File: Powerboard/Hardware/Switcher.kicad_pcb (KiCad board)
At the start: 4 copper layers, 47 x 50 mm, 118 parts, among them IC2 SiC437BED-T1-GE3, J1 Conn_01x03_MountingPin, J2 XT60PW-F, J3 USB_C_Receptacle_USB2.0, J4 Conn_01x02_Male, J5 Conn_01x08_Male, J6 Conn_01x02_Male, J7 XT60PW-M, J8 Conn_01x04_Male, Q1 PXP012-30QLJ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

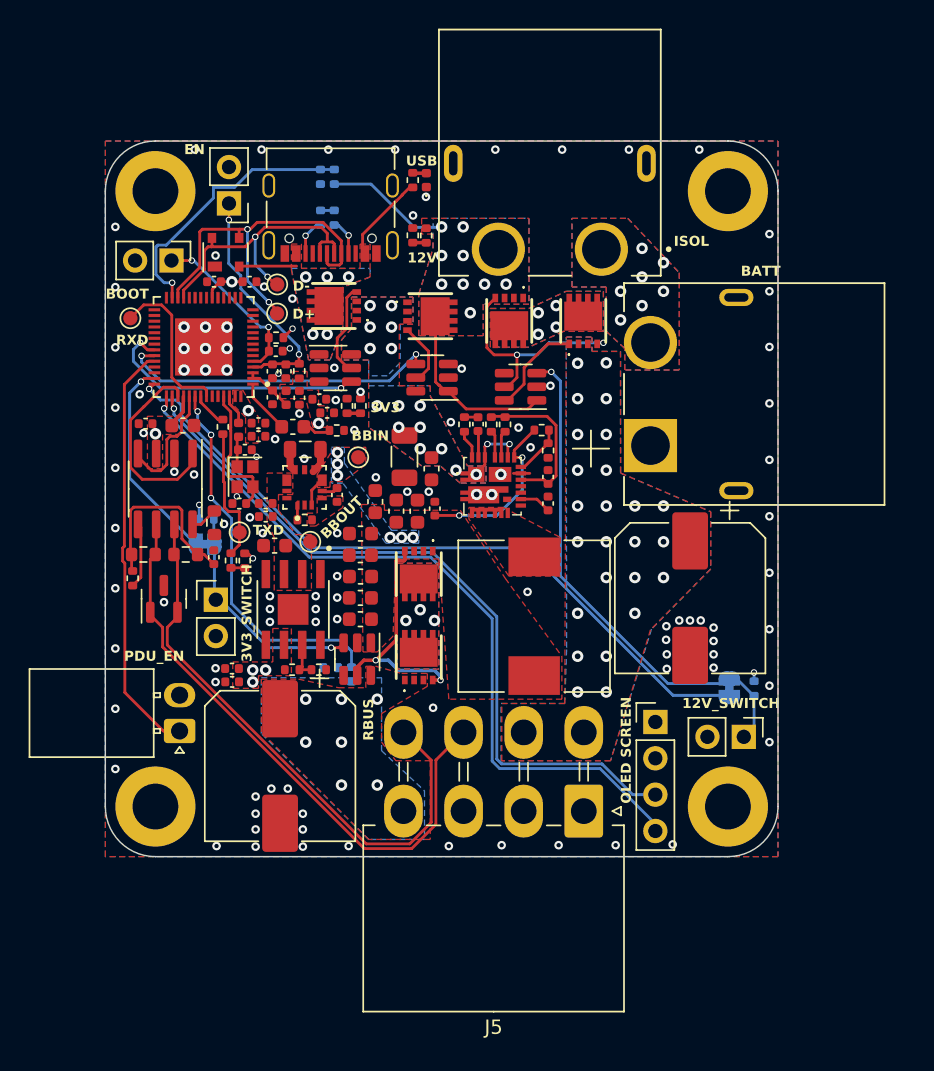
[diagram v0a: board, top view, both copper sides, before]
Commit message: mosfet flipping
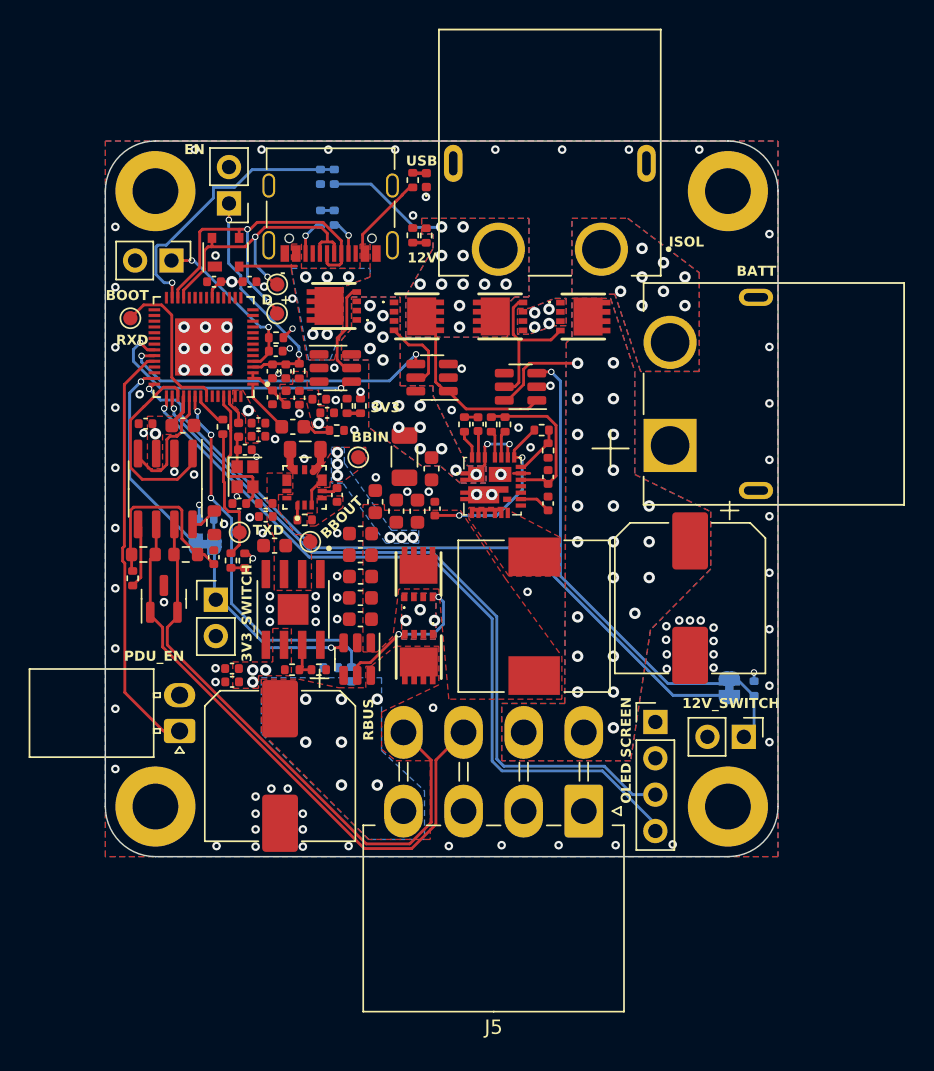
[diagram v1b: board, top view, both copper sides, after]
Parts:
- moved J7 1.37 mm to (112.0, 40.7)
- moved Q5 0.94 mm to (88.3, 35.2)
- moved Q4 0.71 mm to (94.1, 35.3), turned to 90 degrees
- moved Q3 0.31 mm to (99.9, 35.3), turned to -90 degrees
- turned Q2 to 0 degrees
- turned Q1 to 180 degrees
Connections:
- Q1 pad 1: Net-(J5-Pin_4) -> Net-(Q1-S_1)
- Q1 pad 2: Net-(J5-Pin_4) -> Net-(Q1-S_1)
- Q1 pad 3: Net-(J5-Pin_4) -> Net-(Q1-S_1)
- Q1 pad 5: Net-(Q1-D_1) -> Net-(J5-Pin_4)
- Q1 pad 6: Net-(Q1-D_1) -> Net-(J5-Pin_4)
- Q1 pad 7: Net-(Q1-D_1) -> Net-(J5-Pin_4)
- Q1 pad 8: Net-(Q1-D_1) -> Net-(J5-Pin_4)
- Q1 pad 9: Net-(Q1-D_1) -> Net-(J5-Pin_4)
- Q2 pad 1: RBUS_uC_V -> Net-(Q1-S_1)
- Q2 pad 2: RBUS_uC_V -> Net-(Q1-S_1)
- Q2 pad 3: RBUS_uC_V -> Net-(Q1-S_1)
- Q2 pad 5: Net-(Q1-D_1) -> RBUS_uC_V
- Q2 pad 6: Net-(Q1-D_1) -> RBUS_uC_V
- Q2 pad 7: Net-(Q1-D_1) -> RBUS_uC_V
- Q2 pad 8: Net-(Q1-D_1) -> RBUS_uC_V
- Q2 pad 9: Net-(Q1-D_1) -> RBUS_uC_V
- Q3 pad 1: Net-(J5-Pin_5) -> Net-(Q3-S_1)
- Q3 pad 2: Net-(J5-Pin_5) -> Net-(Q3-S_1)
- Q3 pad 3: Net-(J5-Pin_5) -> Net-(Q3-S_1)
- Q3 pad 5: Net-(Q3-D_1) -> Net-(J5-Pin_5)
- Q3 pad 6: Net-(Q3-D_1) -> Net-(J5-Pin_5)
- Q3 pad 7: Net-(Q3-D_1) -> Net-(J5-Pin_5)
- Q3 pad 8: Net-(Q3-D_1) -> Net-(J5-Pin_5)
- Q3 pad 9: Net-(Q3-D_1) -> Net-(J5-Pin_5)
- Q4 pad 1: +12V -> Net-(Q3-S_1)
- Q4 pad 2: +12V -> Net-(Q3-S_1)
- Q4 pad 3: +12V -> Net-(Q3-S_1)
- Q4 pad 5: Net-(Q3-D_1) -> +12V
- Q4 pad 6: Net-(Q3-D_1) -> +12V
- Q4 pad 7: Net-(Q3-D_1) -> +12V
- Q4 pad 8: Net-(Q3-D_1) -> +12V
- Q4 pad 9: Net-(Q3-D_1) -> +12V
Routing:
- net Net-(Q1-G): track 16.7 -> 10.8 mm
- net Net-(Q3-G): track 15.6 -> 10.5 mm, vias 2 -> 0
- net Net-(Q5-G): track 4.44 -> 5.57 mm
- net +12V: track 21.6 -> 21.9 mm, vias 9 -> 11
- net Net-(J5-Pin_5): track 6.85 -> 6.83 mm, vias 25 -> 23
- net Net-(Q3-S_1): vias 0 -> 4
- net Net-(Q3-D_1): vias 4 -> 0
- net Net-(Q1-S_1): vias 0 -> 3
- net Net-(Q1-D_1): vias 3 -> 0
- net Net-(J7--): vias 7 -> 8
- net GND: vias 112 -> 111
- added copper zone on B.Cu, net Net-(Q1-S_1)
- added copper zone on F.Cu, net Net-(Q1-S_1)
- added copper zone on B.Cu, net Net-(Q3-S_1)
- added copper zone on F.Cu, net Net-(Q3-S_1)
- removed copper zone on B.Cu, net Net-(Q1-D_1)
- removed copper zone on F.Cu, net Net-(Q1-D_1)
- removed copper zone on B.Cu, net Net-(Q3-D_1)
- removed copper zone on F.Cu, net Net-(Q3-D_1)
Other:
- board text added: "+"
- board text added: "-"
- board text added: "D"
- board text removed: "D+"
- board text removed: "D-"

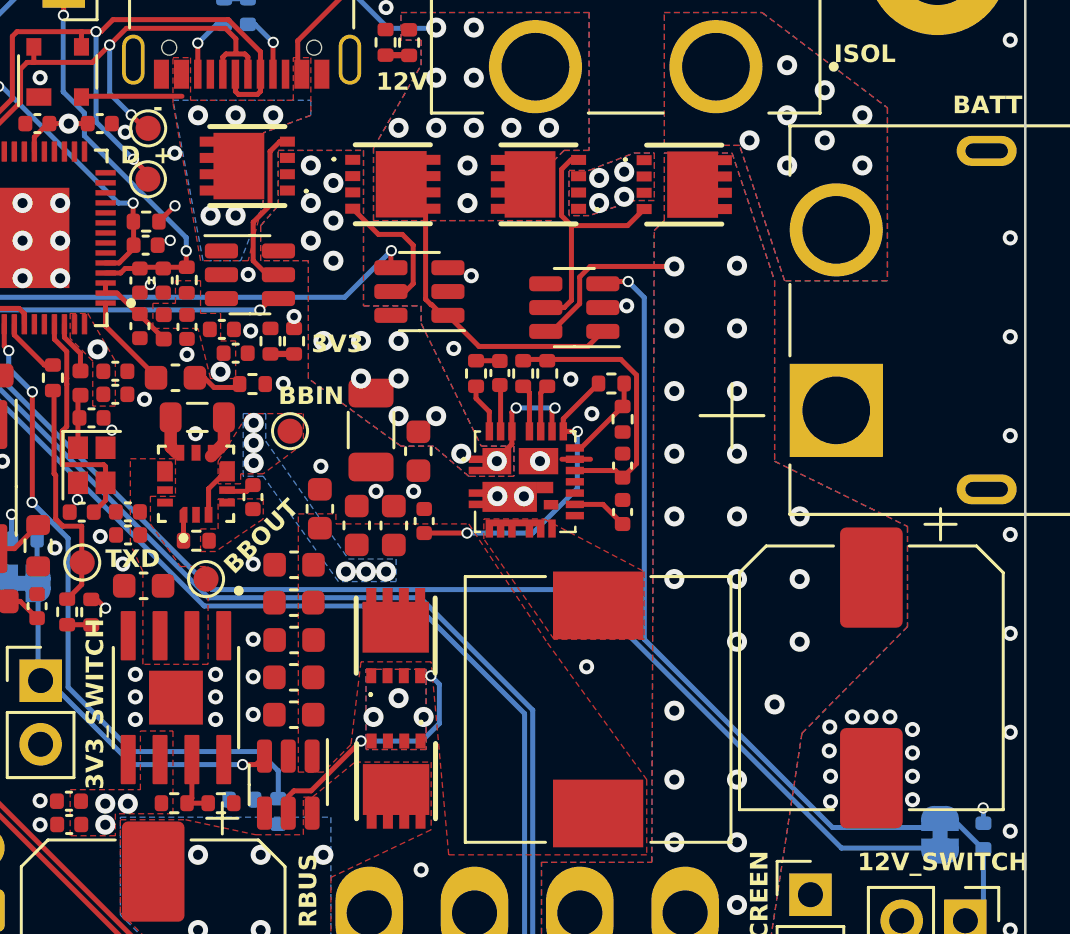
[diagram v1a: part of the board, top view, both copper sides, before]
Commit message: removed 100nf cap, pgood pull up
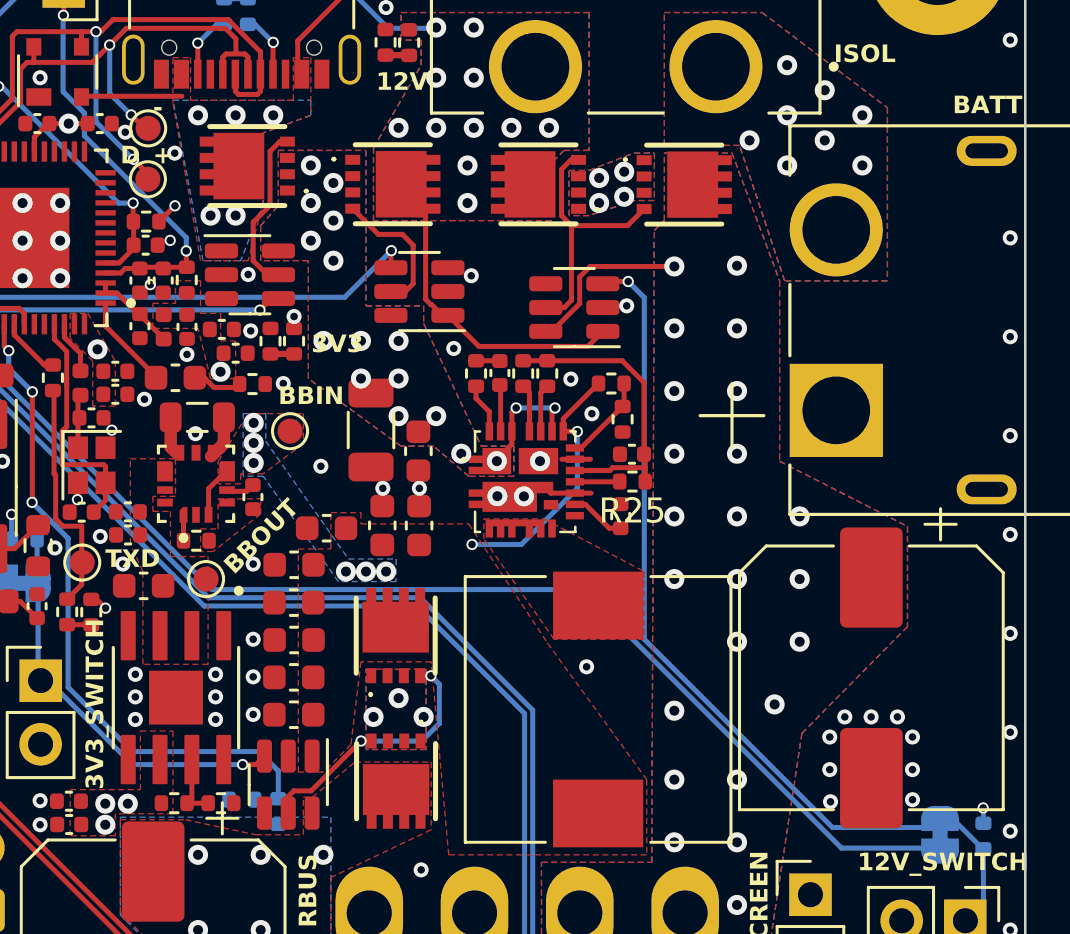
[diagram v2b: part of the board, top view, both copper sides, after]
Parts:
- removed C28: 100nF, Capacitor_SMD:C_0402_1005Metric
- added R25: 10k, Resistor_SMD:R_0402_1005Metric, F.Cu at (97.8, 47.1)
- moved C30 1.02 mm to (87.8, 48.9)
- moved C32 1.01 mm to (89.3, 48.9)
- moved C36 0.82 mm to (85.6, 49.0), turned to 0 degrees
- moved C46 0.59 mm to (97.8, 46.0), turned to 0 degrees
- moved C47 0.18 mm to (97.4, 48.5)
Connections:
- IC2 pad 14: GND -> Net-(IC2-P_GOOD)
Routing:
- net GND: track 2.09 -> 4.02 mm, vias 111 -> 109
- net Net-(IC2-P_GOOD): track 0.00 -> 1.79 mm
- net RBUS_uC_V: track 14.2 -> 12.5 mm
- net /Bucks/Vdd: track 11.1 -> 12.0 mm

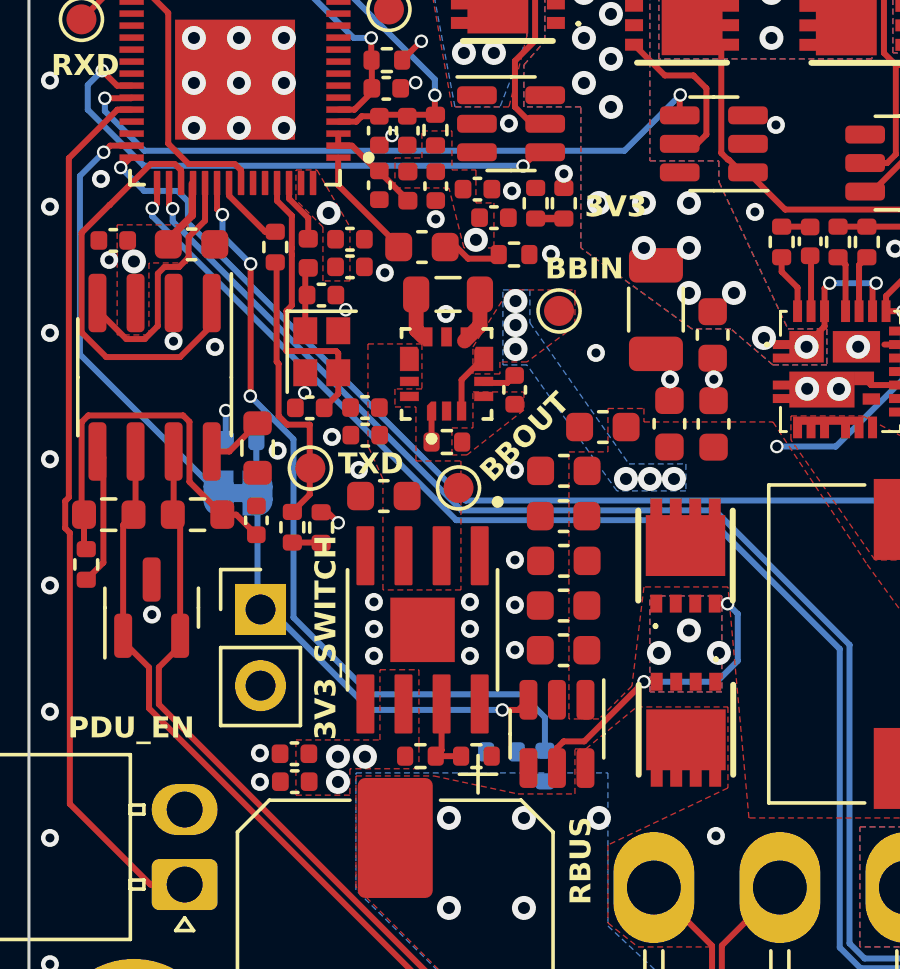
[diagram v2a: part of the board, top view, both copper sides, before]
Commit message: 3v3logging moved to buck output
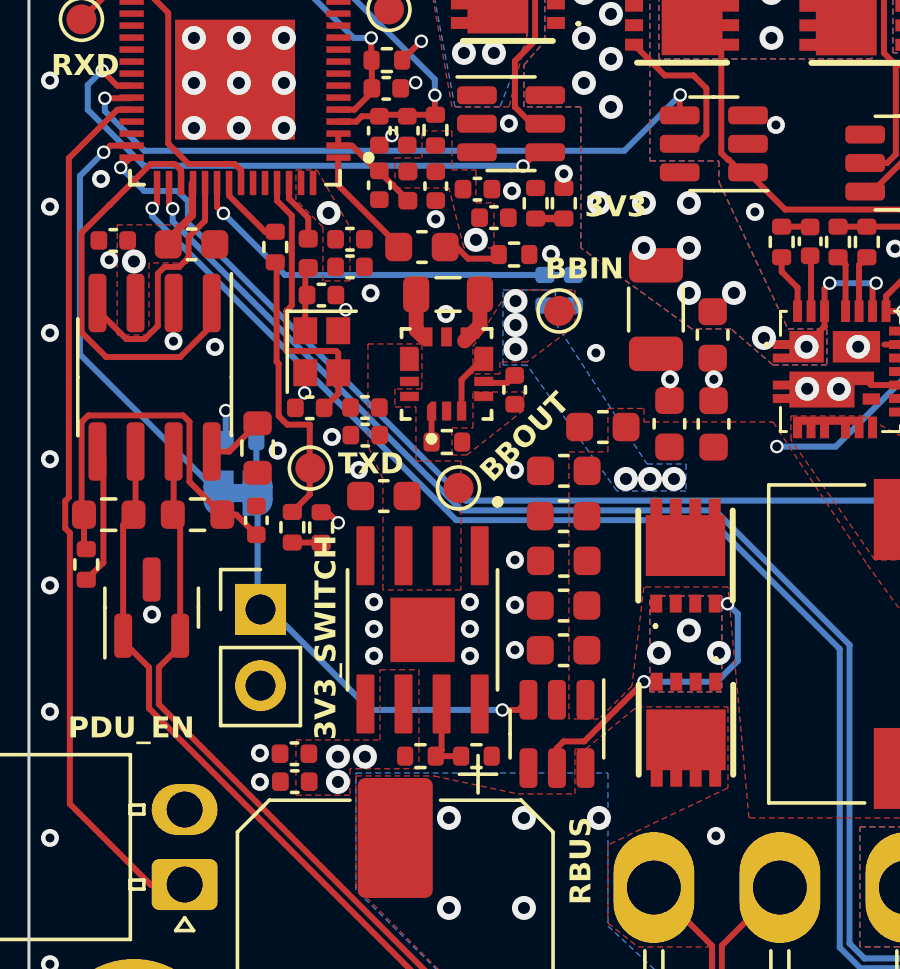
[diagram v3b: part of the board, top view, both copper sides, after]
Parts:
- R24: value R_Small -> 10k
- R26: value R_Small -> 160k
- moved R24 15.9 mm to (83.7, 44.4)
- moved R26 15.6 mm to (84.7, 44.4), turned to -90 degrees
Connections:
- R24 pad 1: Net-(J5-Pin_4) -> RBUS_uC_V
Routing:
- net /3V3LOG: track 27.4 -> 13.6 mm, vias 3 -> 1

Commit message: dumbass
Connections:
- J2 pad 1: Net-(J7--) -> Net-(J7-+)
- J7 pad 1: GND -> Net-(J7-+)
- J7 pad 2: Net-(J7--) -> GND
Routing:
- net Net-(J7--): vias 8 -> 0
- net Net-(J7-+): vias 0 -> 18
- added copper zone on B.Cu, net Net-(J7-+)
- added copper zone on F.Cu, net Net-(J7-+)
- removed copper zone on B.Cu, net Net-(J7--)
- removed copper zone on F.Cu, net Net-(J7--)
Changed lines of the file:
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@@
   (net 27 "Net-(C20-Pad1)")
   (net 28 "/CAN-")
-  (net 29 "Net-(J7--)")
+  (net 29 "Net-(J7-+)")
   (net 30 "/CHIP_PU")
   (net 31 "/BOOT")
@@
       (stroke (width 0.127) (type solid)) (layer "F.Fab"))
     (pad "1" thru_hole rect (at 3.6 6 270) (size 3.716 3.716) (drill 2.7) (layers "*.Cu" "*.Mask")
-      (net 3 "GND") (pinfunction "+") (pintype "passive"))
+      (net 29 "Net-(J7-+)") (pinfunction "+") (pintype "passive"))
     (pad "2" thru_hole circle (at -3.6 6 270) (size 3.716 3.716) (drill 2.7) (layers "*.Cu" "*.Mask")
-      (net 29 "Net-(J7--)") (pinfunction "-") (pintype "passive"))
+      (net 3 "GND") (pinfunction "-") (pintype "passive"))
     (pad "S1" thru_hole oval (at 6.75 0 270) (size 1.2 2.4) (drill oval 0.6 1.7) (layers "*.Cu" "*.Mask"))
     (pad "S2" thru_hole oval (at -6.75 0 270) (size 1.2 2.4) (drill oval 0.6 1.7) (layers "*.Cu" "*.Mask"))
@@
       (stroke (width 0.2) (type solid)) (fill none) (layer "F.Fab"))
     (pad "1" thru_hole circle (at -3.6 0 180) (size 3.716 3.716) (drill 2.7) (layers "*.Cu" "*.Mask")
-      (net 29 "Net-(J7--)") (pinfunction "1") (pintype "passive"))
+      (net 29 "Net-(J7-+)") (pinfunction "1") (pintype "passive"))
     (pad "2" thru_hole circle (at 3.6 0 180) (size 3.716 3.716) (drill 2.7) (layers "*.Cu" "*.Mask")
       (net 2 "+12V") (pinfunction "2") (pintype "passive"))
@@
   (segment (start 70.503 58.347528) (end 84.592472 72.437) (width 0.2) (layer "F.Cu") (net 28))
   (segment (start 69.64 52.235) (end 69.64 55.9275) (width 0.2) (layer "F.Cu") (net 28))
-  (via (at 107 32.5) (size 0.8) (drill 0.4) (layers "F.Cu" "B.Cu") (free) (net 29))
-  (via (at 102.5 33.5) (size 0.8) (drill 0.4) (layers "F.Cu" "B.Cu") (free) (net 29))
-  (via (at 104 32.5) (size 0.8) (drill 0.4) (layers "F.Cu" "B.Cu") (free) (net 29))
-  (via (at 107 34.5) (size 0.8) (drill 0.4) (layers "F.Cu" "B.Cu") (free) (net 29))
+  (via (at 112 44) (size 0.8) (drill 0.4) (layers "F.Cu" "B.Cu") (free) (net 29))
+  (via (at 105.5 41.5) (size 0.8) (drill 0.4) (layers "F.Cu" "B.Cu") (free) (net 29))
+  (via (at 105.5 39.5) (size 0.8) (drill 0.4) (layers "F.Cu" "B.Cu") (free) (net 29))
+  (via (at 108 33.5) (size 0.8) (drill 0.4) (layers "F.Cu" "B.Cu") (free) (net 29))
+  (via (at 110 40.5) (size 0.8) (drill 0.4) (layers "F.Cu" "B.Cu") (free) (net 29))
+  (via (at 108 39.5) (size 0.8) (drill 0.4) (layers "F.Cu" "B.Cu") (free) (net 29))
+  (via (at 103.5 35) (size 0.8) (drill 0.4) (layers "F.Cu" "B.Cu") (free) (net 29))
+  (via (at 112 41.5) (size 0.8) (drill 0.4) (layers "F.Cu" "B.Cu") (free) (net 29))
+  (via (at 110 45.5) (size 0.8) (drill 0.4) (layers "F.Cu" "B.Cu") (free) (net 29))
+  (via (at 112 39) (size 0.8) (drill 0.4) (layers "F.Cu" "B.Cu") (free) (net 29))
+  (via (at 112 36.5) (size 0.8) (drill 0.4) (layers "F.Cu" "B.Cu") (free) (net 29))
+  (via (at 108 41.5) (size 0.8) (drill 0.4) (layers "F.Cu" "B.Cu") (free) (net 29))
   (via (at 105.5 33.5) (size 0.8) (drill 0.4) (layers "F.Cu" "B.Cu") (free) (net 29))
-  (via (at 105.5 31.5) (size 0.8) (drill 0.4) (layers "F.Cu" "B.Cu") (free) (net 29))
-  (via (at 104 30.5) (size 0.8) (drill 0.4) (layers "F.Cu" "B.Cu") (free) (net 29))
-  (via (at 104 34.5) (size 0.8) (drill 0.4) (layers "F.Cu" "B.Cu") (free) (net 29))
+  (via (at 110 38) (size 0.8) (drill 0.4) (layers "F.Cu" "B.Cu") (free) (net 29))
+  (via (at 110 43) (size 0.8) (drill 0.4) (layers "F.Cu" "B.Cu") (free) (net 29))
+  (via (at 105.5 30.5) (size 0.8) (drill 0.4) (layers "F.Cu" "B.Cu") (free) (net 29))
+  (via (at 103.5 32) (size 0.8) (drill 0.4) (layers "F.Cu" "B.Cu") (free) (net 29))
+  (via (at 103.5 29) (size 0.8) (drill 0.4) (layers "F.Cu" "B.Cu") (free) (net 29))
   (segment (start 76.8075 38.79) (end 77.412448 38.79) (width 0.2) (layer "F.Cu") (net 30))
   (segment (start 77.412448 38.79) (end 77.592448 38.61) (width 0.2) (layer "F.Cu") (net 30))
@@
     )
   )
+  (zone (net 29) (net_name "Net-(J7-+)") (layers "F&B.Cu") (hatch edge 0.5)
+    (priority 7)
+    (connect_pads yes (clearance 0.254))
+    (min_thickness 0.25) (filled_areas_thickness no)
+    (fill yes (thermal_gap 0.5) (thermal_bridge_width 0.5))
+    (polygon
+      (pts
+        (xy 104 46.2)
+        (xy 112.3 46.2)
+        (xy 112.4 36.6)
+        (xy 105.3 28.2)
+        (xy 99 28.2)
+        (xy 99 33.6)
+        (xy 101.9 33.6)
+        (xy 104 39.1)
+      )
+    )
+  )
   (zone (net 2) (net_name "+12V") (layers "F&B.Cu") (hatch edge 0.508)
     (priority 1)
@@
       )
     )
-  )
-  (zone (net 29) (net_name "Net-(J7--)") (layers "F&B.Cu") (hatch edge 0.508)
-    (priority 1)
-    (connect_pads yes (clearance 0.254))
-    (min_thickness 0.254) (filled_areas_thickness no)
-    (fill yes (thermal_gap 0.508) (thermal_bridge_width 0.508))
-    (polygon
-      (pts
-        (xy 108 32.2)
-        (xy 108 39.1)
-        (xy 103.9 39.1)
-        (xy 102.1 33.7)
-        (xy 99.1 33.7)
-        (xy 99.1 28.4)
-        (xy 103 28.4)
-      )
-    )
